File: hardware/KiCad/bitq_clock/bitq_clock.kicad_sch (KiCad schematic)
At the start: 3 parts, among them U1 ICM7555xP, U2 ICM7555xP, U3 ICM7555xP

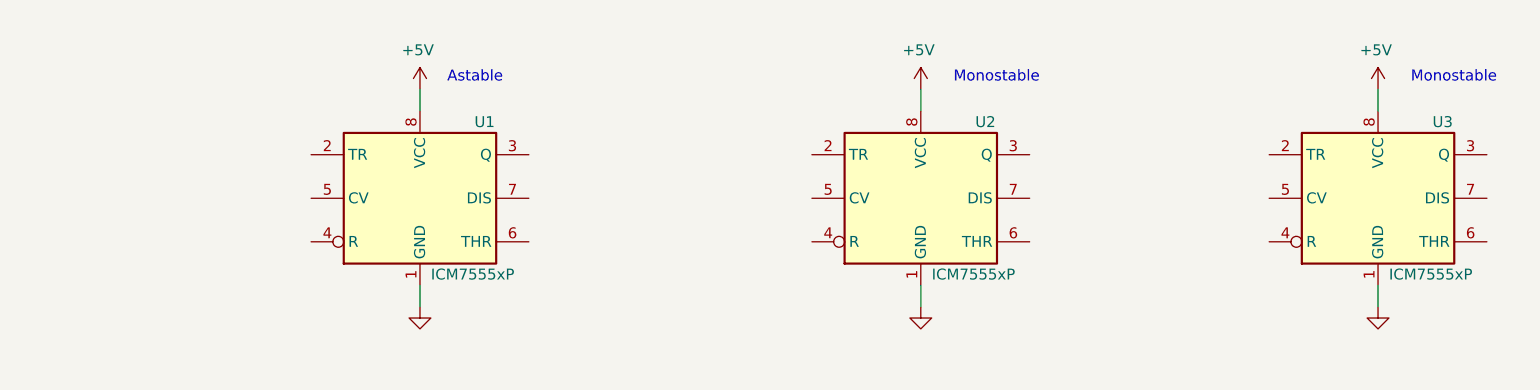
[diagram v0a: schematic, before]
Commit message: feat: hardware: Adds astable clock #1
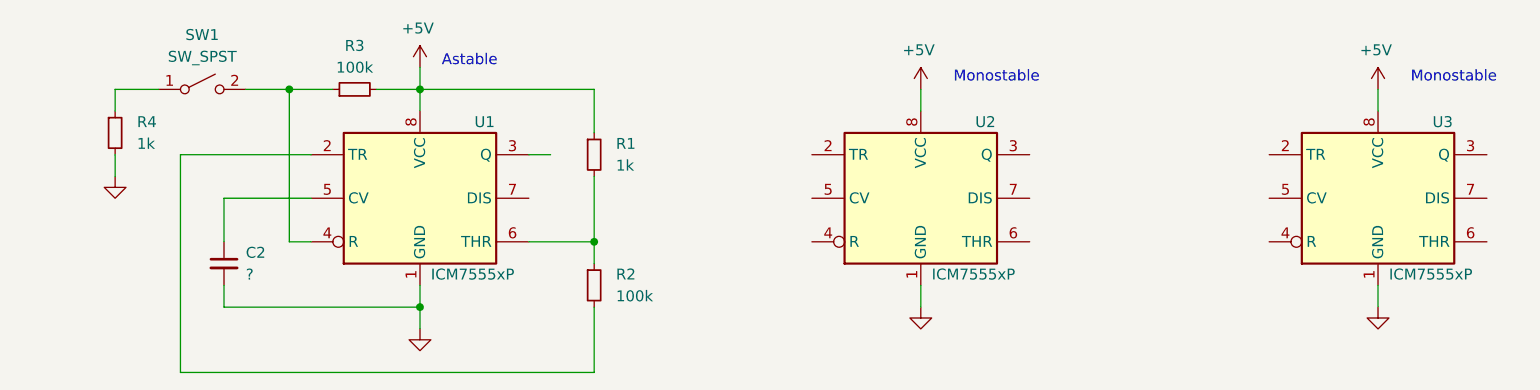
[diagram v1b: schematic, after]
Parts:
- added C2: ?, symbol Device:C_Small
- added R1, R4: 1k, symbol Device:R_Small
- added R2, R3: 100k, symbol Device:R_Small
- added SW1: SW_SPST, symbol Switch:SW_SPST
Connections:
- net +5V: now also R1.1, R3.2
- net GND: now also C2.2, R4.2
- net at U1.2 (TR): now also R2.2
- net at U1.4 (R): now also R3.1, SW1.2 (B)
- net at U1.5 (CV): now also C2.1
- net at U1.6 (THR): now also R1.2, R2.1
- new net: R4.1, SW1.1 (A)

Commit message: feat: hardware: Adds astable clock #2
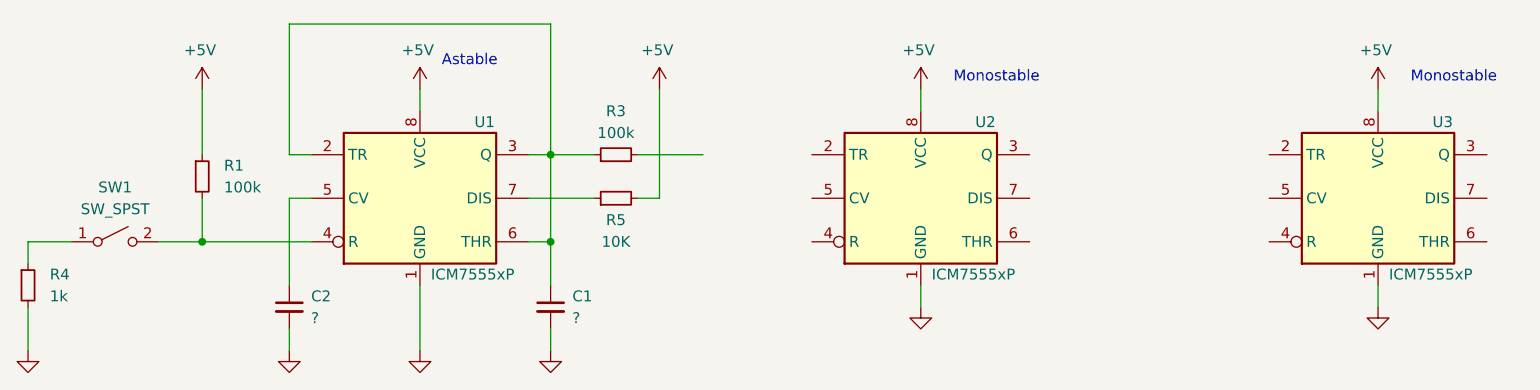
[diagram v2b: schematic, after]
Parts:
- removed R2: 100k, symbol Device:R_Small
- added C1: ?, symbol Device:C_Small
- added R5: 10K, symbol Device:R_Small
- R1: value 1k -> 100k
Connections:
- net +5V: now also R5.2; no longer R3.2
- net GND: now also C1.2
- net at SW1.2 (B), U1.4 (R): now also R1.2; no longer R3.1
- net at U1.6 (THR): now also R3.1, U1.2 (TR), U1.3 (Q), C1.1; no longer R1.2
- net at U1.7 (DIS): now also R5.1
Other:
- moved on the sheet: C2, R4, SW1
